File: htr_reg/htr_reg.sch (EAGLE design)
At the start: 20 parts, among them J1 XT30_EDGE, J2 XT30_EDGE, J3 XT30_EDGE, U1 TLV3691_SC70-5, U2 TLV3691_SC70-5

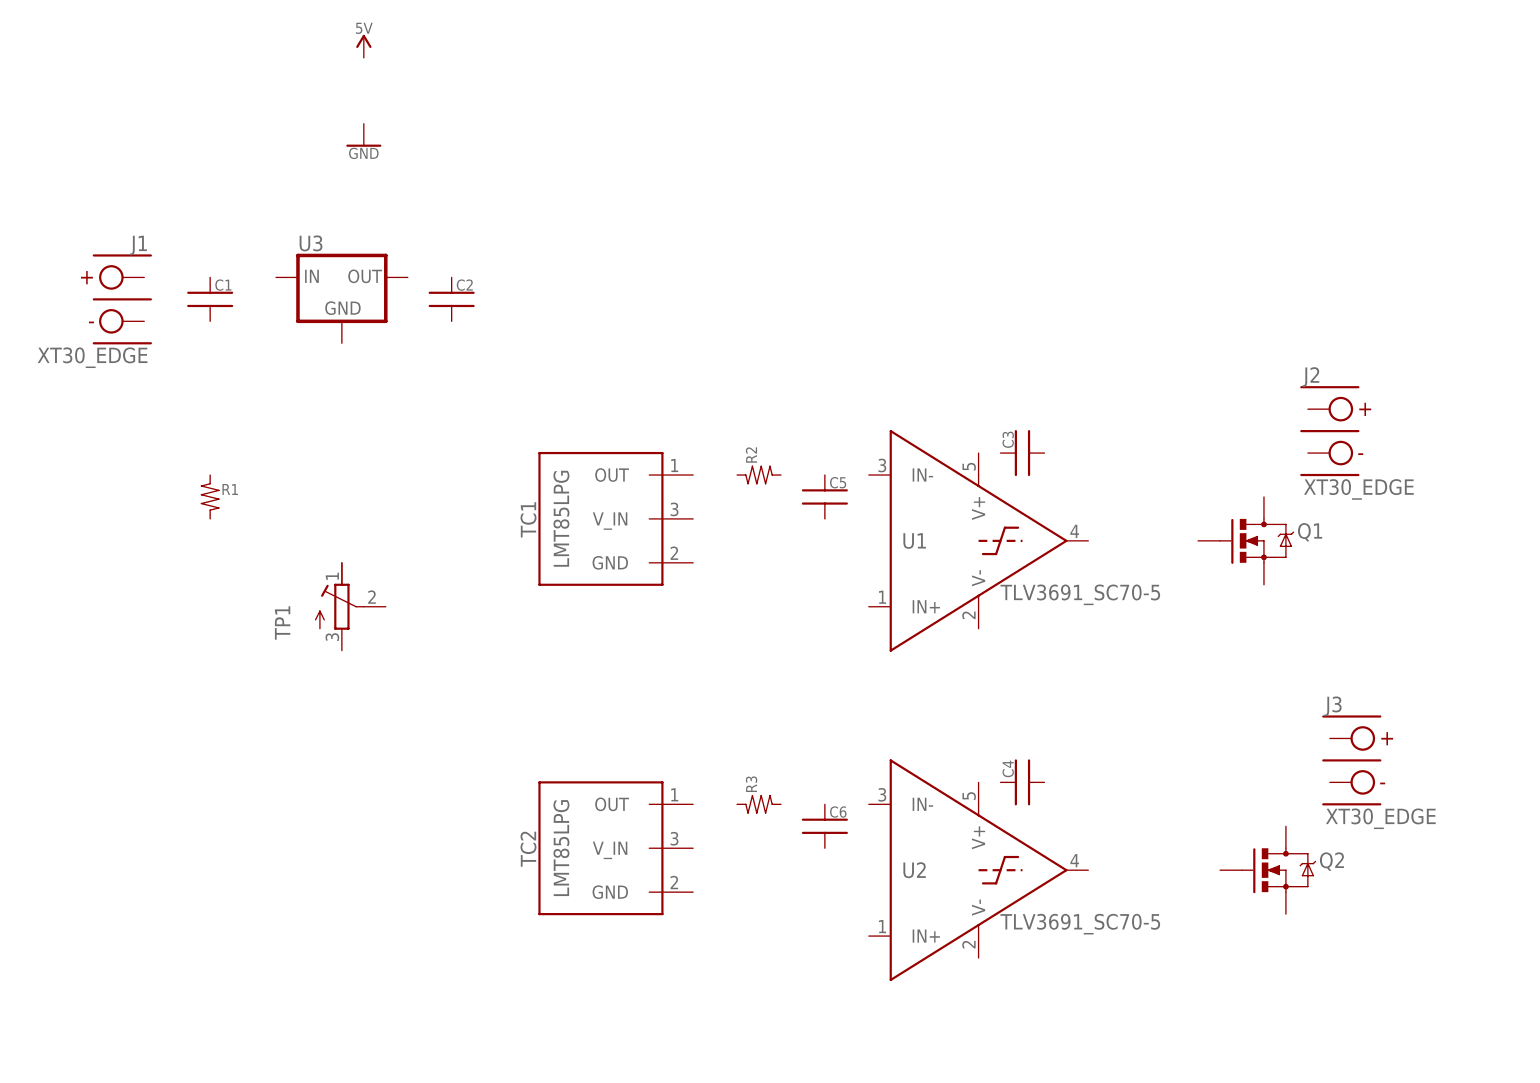
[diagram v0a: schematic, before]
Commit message: organized and connected the schematic
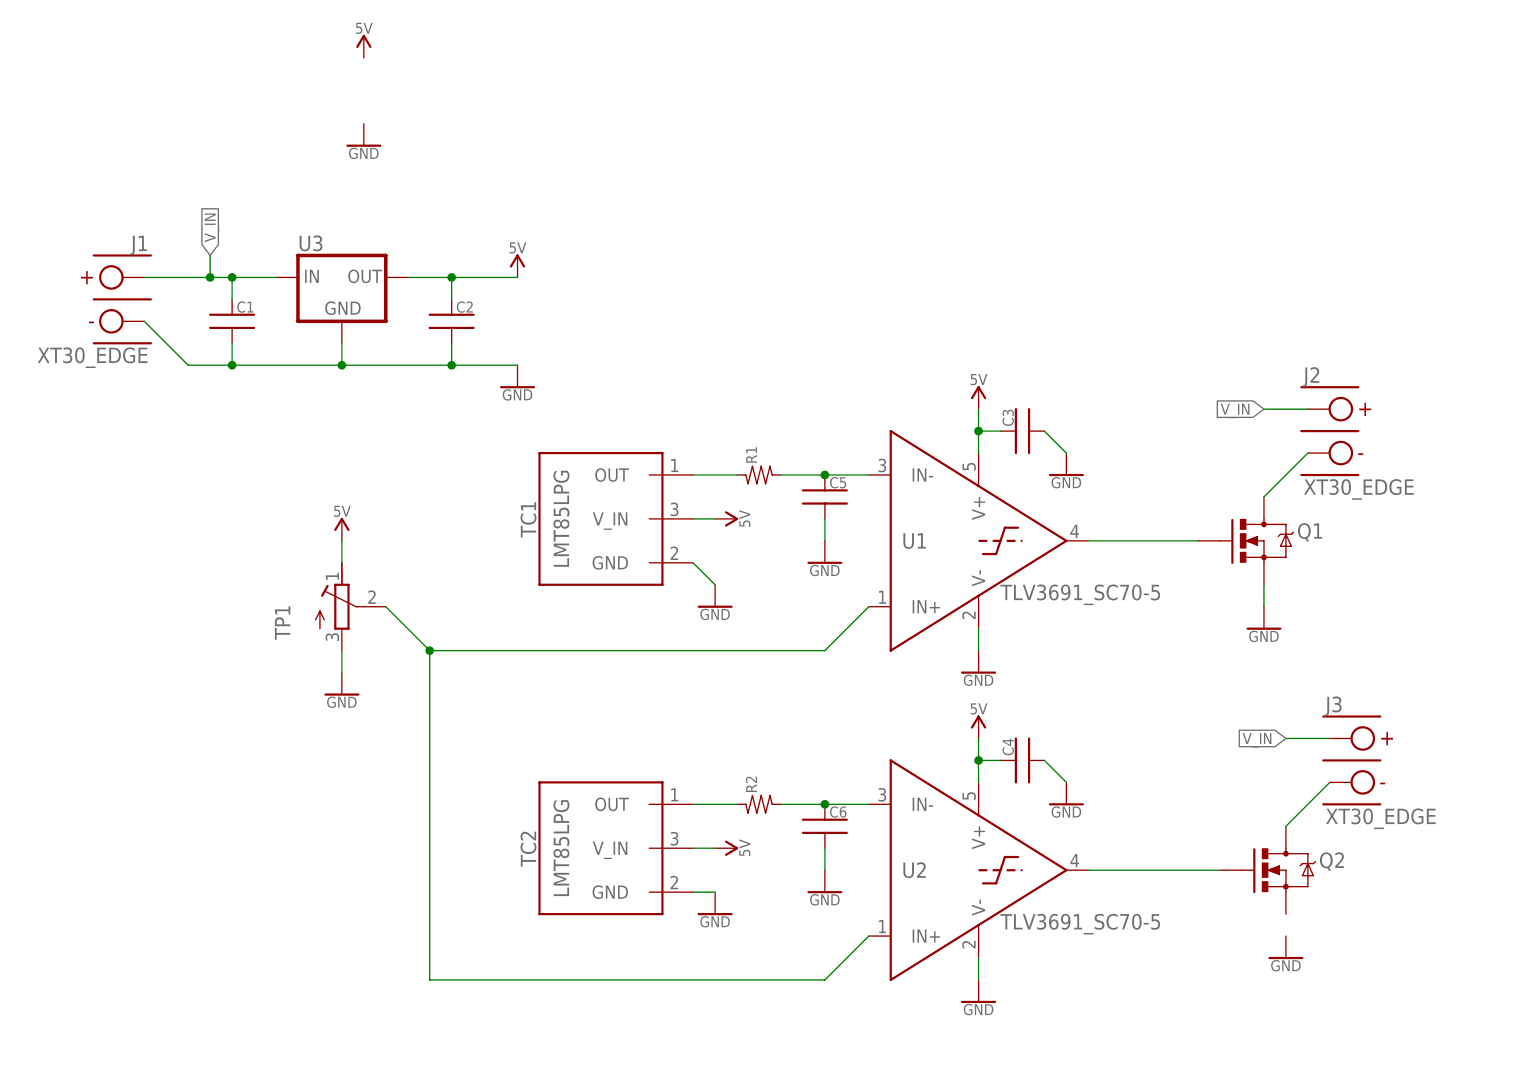
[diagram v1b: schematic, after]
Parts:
- removed R3: (no value), htr_reg_lib:RES_SMD0603
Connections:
- new net 5V: C2.1, C3.1, C4.1, TC1.V_IN, TC2.V_IN, TP1.E, U1.V+, U2.V+, U3.OUT
- new net GND: C1.2, C2.2, C3.2, C4.2, C5.2, C6.2, J1.NEG, Q1.S, TC1.GND, TC2.GND, TP1.A, U1.V-, U2.V-, U3.GND
- new net N$10: R1.1, TC1.OUT
- new net N$11: TP1.S, U1.IN+, U2.IN+
- new net N$3: Q2.G, U2.OUT
- new net N$4: Q1.G, U1.OUT
- new net N$5: J3.NEG, Q2.D
- new net N$6: J2.NEG, Q1.D
- new net N$7: C6.1, R2.2, U2.IN-
- new net N$8: R2.1, TC2.OUT
- new net N$9: C5.1, R1.2, U1.IN-
- new net V_IN: C1.1, J1.POS, J2.POS, J3.POS, U3.IN
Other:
- moved on the sheet: C1, C2, C3, C4, R1, R2

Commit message: Added and twiddled small bits of the lib. Routed traces on the board, possibly finished.
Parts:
- added D1, D2: (no value), htr_reg_lib:LED0603
- added R3, R4: (no value), htr_reg_lib:RES_SMD0603
- TC1, TC2: value LMT85LPG -> LMT85.1"; device htr_reg_lib:LMT85LPG -> htr_reg_lib:LMT85.1"
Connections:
- net N$10 renamed FB_A
- net N$11 renamed SET
- net N$8 renamed FB_B
- removed net N$3: Q2.G, U2.OUT
- new net N$2: D1.C, R3.1
- new net OUT_A: D1.A, Q1.G, U1.OUT
- new net OUT_B: D2.A, Q2.G, U2.OUT
- net GND: now also Q2.S, R3.2, R4.2
- net N$4: now also D2.C, R4.1; no longer Q1.G, U1.OUT
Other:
- moved on the sheet: J2, J3, Q1, Q2
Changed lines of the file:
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@@
 <part name="GND1" library="htr_reg_lib" deviceset="GND" device=""/>
 <part name="C2" library="htr_reg_lib" deviceset="CAP_SMD" device="_0603"/>
-<part name="TC1" library="htr_reg_lib" deviceset="LMT85" device="LPG"/>
-<part name="TC2" library="htr_reg_lib" deviceset="LMT85" device="LPG"/>
+<part name="TC1" library="htr_reg_lib" deviceset="LMT85" device=".1&quot;" value="LMT85.1&quot;"/>
+<part name="TC2" library="htr_reg_lib" deviceset="LMT85" device=".1&quot;" value="LMT85.1&quot;"/>
 <part name="C3" library="htr_reg_lib" deviceset="CAP_SMD" device="_0603"/>
 <part name="C4" library="htr_reg_lib" deviceset="CAP_SMD" device="_0603"/>
@@
 <part name="SUPPLY7" library="htr_reg_lib" deviceset="5V" device=""/>
 <part name="GND13" library="htr_reg_lib" deviceset="GND" device=""/>
+<part name="D1" library="htr_reg_lib" deviceset="LED" device="0603"/>
+<part name="D2" library="htr_reg_lib" deviceset="LED" device="0603"/>
+<part name="R3" library="htr_reg_lib" deviceset="RES_SMD" device="0603"/>
+<part name="R4" library="htr_reg_lib" deviceset="RES_SMD" device="0603"/>
+<part name="GND14" library="htr_reg_lib" deviceset="GND" device=""/>
+<part name="GND15" library="htr_reg_lib" deviceset="GND" device=""/>
 </parts>
 <sheets>
@@
 <instances>
 <instance part="J1" gate="G$1" x="38.1" y="86.36"/>
-<instance part="J2" gate="G$1" x="172.72" y="71.12" rot="MR0"/>
-<instance part="J3" gate="G$1" x="175.26" y="33.02" rot="MR0"/>
-<instance part="Q1" gate="G$1" x="167.64" y="58.42"/>
-<instance part="Q2" gate="G$1" x="170.18" y="20.32"/>
+<instance part="J2" gate="G$1" x="182.88" y="71.12" rot="MR0"/>
+<instance part="J3" gate="G$1" x="182.88" y="33.02" rot="MR0"/>
+<instance part="Q1" gate="G$1" x="177.8" y="58.42"/>
+<instance part="Q2" gate="G$1" x="177.8" y="20.32"/>
 <instance part="C1" gate="G$1" x="48.26" y="83.82"/>
 <instance part="U1" gate="G$1" x="132.08" y="58.42"/>
@@
 <instance part="GND3" gate="1" x="144.78" y="27.94"/>
 <instance part="GND4" gate="1" x="134.62" y="5.08"/>
-<instance part="GND5" gate="1" x="170.18" y="10.16"/>
-<instance part="GND6" gate="1" x="167.64" y="48.26"/>
+<instance part="GND5" gate="1" x="177.8" y="10.16"/>
+<instance part="GND6" gate="1" x="177.8" y="48.26"/>
 <instance part="GND7" gate="1" x="104.14" y="50.8"/>
 <instance part="GND8" gate="1" x="104.14" y="15.24"/>
@@
 <instance part="SUPPLY7" gate="G$1" x="60.96" y="58.42"/>
 <instance part="GND13" gate="1" x="60.96" y="40.64"/>
+<instance part="D1" gate="G$1" x="165.1" y="53.34"/>
+<instance part="D2" gate="G$1" x="165.1" y="15.24"/>
+<instance part="R3" gate="G$1" x="165.1" y="45.72"/>
+<instance part="R4" gate="G$1" x="165.1" y="7.62"/>
+<instance part="GND14" gate="1" x="165.1" y="38.1"/>
+<instance part="GND15" gate="1" x="165.1" y="0"/>
 </instances>
 <busses>
@@
 <pinref part="Q1" gate="G$1" pin="S"/>
 <pinref part="GND6" gate="1" pin="GND"/>
-<wire x1="167.64" y1="53.34" x2="167.64" y2="50.8" width="0.1524" layer="91"/>
+<wire x1="177.8" y1="53.34" x2="177.8" y2="50.8" width="0.1524" layer="91"/>
 </segment>
 <segment>
@@
 <pinref part="GND13" gate="1" pin="GND"/>
 <wire x1="60.96" y1="45.72" x2="60.96" y2="43.18" width="0.1524" layer="91"/>
+</segment>
+<segment>
+<pinref part="GND5" gate="1" pin="GND"/>
+<pinref part="Q2" gate="G$1" pin="S"/>
+<wire x1="177.8" y1="12.7" x2="177.8" y2="15.24" width="0.1524" layer="91"/>
+</segment>
+<segment>
+<pinref part="R3" gate="G$1" pin="2"/>
+<pinref part="GND14" gate="1" pin="GND"/>
+<wire x1="165.1" y1="43.18" x2="165.1" y2="40.64" width="0.1524" layer="91"/>
+</segment>
+<segment>
+<pinref part="R4" gate="G$1" pin="2"/>
+<pinref part="GND15" gate="1" pin="GND"/>
+<wire x1="165.1" y1="5.08" x2="165.1" y2="2.54" width="0.1524" layer="91"/>
 </segment>
 </net>
@@
 <segment>
 <pinref part="J2" gate="G$1" pin="POS"/>
-<wire x1="172.72" y1="73.66" x2="167.64" y2="73.66" width="0.1524" layer="91"/>
-<label x="167.64" y="73.66" size="1.27" layer="95" rot="R180" xref="yes"/>
+<wire x1="182.88" y1="73.66" x2="177.8" y2="73.66" width="0.1524" layer="91"/>
+<label x="177.8" y="73.66" size="1.27" layer="95" rot="R180" xref="yes"/>
 </segment>
 <segment>
 <pinref part="J3" gate="G$1" pin="POS"/>
-<wire x1="175.26" y1="35.56" x2="170.18" y2="35.56" width="0.1524" layer="91"/>
-<label x="170.18" y="35.56" size="1.27" layer="95" rot="R180" xref="yes"/>
-</segment>
-</net>
-<net name="N$3" class="0">
+<wire x1="182.88" y1="35.56" x2="177.8" y2="35.56" width="0.1524" layer="91"/>
+<label x="177.8" y="35.56" size="1.27" layer="95" rot="R180" xref="yes"/>
+</segment>
+</net>
+<net name="OUT_B" class="0">
 <segment>
 <pinref part="U2" gate="G$1" pin="OUT"/>
 <pinref part="Q2" gate="G$1" pin="G"/>
-<wire x1="147.32" y1="20.32" x2="162.56" y2="20.32" width="0.1524" layer="91"/>
-</segment>
-</net>
-<net name="N$4" class="0">
-<segment>
-<pinref part="Q1" gate="G$1" pin="G"/>
-<pinref part="U1" gate="G$1" pin="OUT"/>
-<wire x1="160.02" y1="58.42" x2="147.32" y2="58.42" width="0.1524" layer="91"/>
+<wire x1="147.32" y1="20.32" x2="149.86" y2="20.32" width="0.1524" layer="91"/>
+<pinref part="D2" gate="G$1" pin="A"/>
+<wire x1="149.86" y1="20.32" x2="165.1" y2="20.32" width="0.1524" layer="91"/>
+<wire x1="165.1" y1="20.32" x2="170.18" y2="20.32" width="0.1524" layer="91"/>
+<wire x1="165.1" y1="17.78" x2="165.1" y2="20.32" width="0.1524" layer="91"/>
+<junction x="165.1" y="20.32"/>
+<wire x1="149.86" y1="20.32" x2="149.86" y2="22.86" width="0.1524" layer="91"/>
+<junction x="149.86" y="20.32"/>
+<label x="149.86" y="22.86" size="1.27" layer="95" rot="R90" xref="yes"/>
 </segment>
 </net>
@@
 <pinref part="Q2" gate="G$1" pin="D"/>
 <pinref part="J3" gate="G$1" pin="NEG"/>
-<wire x1="170.18" y1="25.4" x2="175.26" y2="30.48" width="0.1524" layer="91"/>
+<wire x1="177.8" y1="25.4" x2="182.88" y2="30.48" width="0.1524" layer="91"/>
 </segment>
 </net>
@@
 <pinref part="Q1" gate="G$1" pin="D"/>
 <pinref part="J2" gate="G$1" pin="NEG"/>
-<wire x1="167.64" y1="63.5" x2="172.72" y2="68.58" width="0.1524" layer="91"/>
+<wire x1="177.8" y1="63.5" x2="182.88" y2="68.58" width="0.1524" layer="91"/>
 </segment>
 </net>
@@
 </segment>
 </net>
-<net name="N$8" class="0">
+<net name="FB_B" class="0">
 <segment>
 <pinref part="R2" gate="G$1" pin="1"/>
 <pinref part="TC2" gate="G$1" pin="OUT"/>
-<wire x1="106.68" y1="27.94" x2="101.6" y2="27.94" width="0.1524" layer="91"/>
+<wire x1="106.68" y1="27.94" x2="104.14" y2="27.94" width="0.1524" layer="91"/>
+<wire x1="104.14" y1="27.94" x2="101.6" y2="27.94" width="0.1524" layer="91"/>
+<wire x1="104.14" y1="27.94" x2="104.14" y2="30.48" width="0.1524" layer="91"/>
+<junction x="104.14" y="27.94"/>
+<label x="104.14" y="30.48" size="1.27" layer="95" rot="R90" xref="yes"/>
 </segment>
 </net>
@@
 </segment>
 </net>
-<net name="N$10" class="0">
+<net name="FB_A" class="0">
 <segment>
 <pinref part="R1" gate="G$1" pin="1"/>
 <pinref part="TC1" gate="G$1" pin="OUT"/>
-<wire x1="106.68" y1="66.04" x2="101.6" y2="66.04" width="0.1524" layer="91"/>
-</segment>
-</net>
-<net name="N$11" class="0">
+<wire x1="106.68" y1="66.04" x2="104.14" y2="66.04" width="0.1524" layer="91"/>
+<wire x1="104.14" y1="66.04" x2="101.6" y2="66.04" width="0.1524" layer="91"/>
+<wire x1="104.14" y1="66.04" x2="104.14" y2="68.58" width="0.1524" layer="91"/>
+<junction x="104.14" y="66.04"/>
+<label x="104.14" y="68.58" size="1.27" layer="95" rot="R90" xref="yes"/>
+</segment>
+</net>
+<net name="SET" class="0">
 <segment>
 <pinref part="U1" gate="G$1" pin="IN+"/>
@@
 <wire x1="66.04" y1="50.8" x2="71.12" y2="45.72" width="0.1524" layer="91"/>
 <junction x="71.12" y="45.72"/>
-</segment>
-</net>
+<wire x1="66.04" y1="50.8" x2="71.12" y2="50.8" width="0.1524" layer="91"/>
+<junction x="66.04" y="50.8"/>
+<label x="71.12" y="50.8" size="1.27" layer="95" xref="yes"/>
+</segment>
+</net>
+<net name="OUT_A" class="0">
+<segment>
+<pinref part="U1" gate="G$1" pin="OUT"/>
+<pinref part="Q1" gate="G$1" pin="G"/>
+<wire x1="147.32" y1="58.42" x2="149.86" y2="58.42" width="0.1524" layer="91"/>
+<pinref part="D1" gate="G$1" pin="A"/>
+<wire x1="149.86" y1="58.42" x2="165.1" y2="58.42" width="0.1524" layer="91"/>
+<wire x1="165.1" y1="58.42" x2="170.18" y2="58.42" width="0.1524" layer="91"/>
+<wire x1="165.1" y1="55.88" x2="165.1" y2="58.42" width="0.1524" layer="91"/>
+<junction x="165.1" y="58.42"/>
+<wire x1="149.86" y1="58.42" x2="149.86" y2="60.96" width="0.1524" layer="91"/>
+<junction x="149.86" y="58.42"/>
+<label x="149.86" y="60.96" size="1.27" layer="95" rot="R90" xref="yes"/>
+</segment>
+</net>
+<net name="N$2" class="0">
+<segment>
+<pinref part="D1" gate="G$1" pin="C"/>
+<pinref part="R3" gate="G$1" pin="1"/>
+<wire x1="165.1" y1="50.8" x2="165.1" y2="48.26" width="0.1524" layer="91"/>
+</segment>
+</net>
+<net name="N$4" class="0">
+<segment>
+<pinref part="D2" gate="G$1" pin="C"/>
+<pinref part="R4" gate="G$1" pin="1"/>
+<wire x1="165.1" y1="12.7" x2="165.1" y2="10.16" width="0.1524" layer="91"/>
+</segment>
+</net>
